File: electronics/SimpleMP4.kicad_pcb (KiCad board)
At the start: 2 copper layers, 126.5 x 65.9 mm, 123 parts, among them J1 USB_OTG, J2 DISPLAY, Q1 8050, Q2 SI2305, Q3 SI2305, Q4 8050, Q5 8550, Q6 SI2305, Q7 8550, U1 OCP8020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

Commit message: added another data bus
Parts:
- removed RN1: 5R, Resistors_THT:R_Array_SIP5
- added R37: 33R, Resistors_SMD:R_0603, F.Cu at (230.8, 226.2)
- added R38: 33R, Resistors_SMD:R_0603, F.Cu at (226.6, 230.7)
- added R39: 33R, Resistors_SMD:R_0603, F.Cu at (235.7, 220.8)
- added R40: 33R, Resistors_SMD:R_0603, F.Cu at (222.6, 235.9)
- added R41: R*, Resistors_SMD:R_0603, F.Cu at (229.8, 231.1)
- added R42: R*, Resistors_SMD:R_0603, F.Cu at (225.8, 235.9)
- added R43: R*, Resistors_SMD:R_0603, F.Cu at (218.0, 242.8)
- added R44: R*, Resistors_SMD:R_0603, F.Cu at (238.9, 220.8)
- added TP1: TEST, Connectors:PINTST, F.Cu at (190.8, 242.5)
- added TP2: TEST, Connectors:PINTST, F.Cu at (219.2, 225.9)
- added TP3: TEST, Connectors:PINTST, F.Cu at (194.5, 242.5)
- added TP4: TEST, Connectors:PINTST, F.Cu at (198.2, 242.5)
- added TP5: TEST, Connectors:PINTST, F.Cu at (232.2, 216.0)
- added TP6: TEST, Connectors:PINTST, F.Cu at (215.1, 232.9)
- added TP7: TEST, Connectors:PINTST, F.Cu at (222.9, 225.9)
- added TP8: TEST, Connectors:PINTST, F.Cu at (219.2, 231.1)
- added TP9: TEST, Connectors:PINTST, F.Cu at (232.2, 221.2)
- B1, B2, B3, B4, B5, B6: footprint SKHLAAA010:SKHLAAA010 -> HP0315AFKP4-R:SW_HP0315AFKP4-R; moved to B.Cu
- moved R36 189.1 mm to (219.3, 236.1)
- moved Q7 179.1 mm to (215.3, 226.8)
- moved B6 176.4 mm to (79.6, 183.0), turned to 270 degrees
- moved R35 173.2 mm to (214.8, 242.8)
- moved C47 169.1 mm to (223.0, 231.0)
- moved C46 164.2 mm to (236.3, 215.9)
- moved C44 163.7 mm to (215.5, 237.9)
- moved B5 160.1 mm to (89.8, 183.0), turned to 270 degrees
- moved U5 159.4 mm to (197.1, 216.8)
- moved C43 157.2 mm to (226.9, 225.8)
- moved B4 143.7 mm to (99.9, 183.0), turned to 270 degrees
- moved B1 133.9 mm to (130.4, 183.0), turned to 90 degrees
- moved B3 127.8 mm to (110.1, 183.0), turned to 270 degrees
- moved B2 115.0 mm to (120.3, 183.0), turned to 270 degrees
- moved J2 95.4 mm to (72.0, 157.6)
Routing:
- net /D0: track 0.00 -> 41.7 mm, vias 0 -> 1
- net /D2: track 0.00 -> 41.6 mm, vias 0 -> 1
- net /D1: track 0.00 -> 40.9 mm, vias 0 -> 1
- net /D3: track 0.00 -> 40.9 mm, vias 0 -> 1
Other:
- board size 126.5 x 65.9 mm -> 130.7 x 66.4 mm

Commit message: routed more of it
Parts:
- moved C43 185.8 mm to (65.4, 134.1), turned to 270 degrees
- moved R35 185.5 mm to (68.2, 129.3), turned to 180 degrees
- moved R36 182.0 mm to (68.1, 134.7), turned to 180 degrees
- moved R39 180.9 mm to (68.6, 151.5), turned to 180 degrees
- moved R44 180.5 mm to (68.6, 161.2), turned to 180 degrees
- moved R37 179.8 mm to (68.6, 148.5), turned to 180 degrees
- moved R41 177.6 mm to (68.6, 156.6), turned to 180 degrees
- moved R38 177.5 mm to (68.6, 150.0), turned to 180 degrees
- moved R42 175.4 mm to (68.6, 158.1), turned to 180 degrees
- moved Q7 175.0 mm to (68.2, 132.1)
- moved R40 174.9 mm to (68.6, 153.0), turned to 180 degrees
- moved R43 171.1 mm to (68.6, 159.6), turned to 180 degrees
- moved U5 13.6 mm to (183.5, 218.1)
- moved C3 3.44 mm to (112.6, 153.4), turned to 90 degrees
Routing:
- net /LCDRDN: track 0.00 -> 116.9 mm, vias 0 -> 2
- net /LCDWRN: track 0.00 -> 114.1 mm, vias 0 -> 2
- net /FALE/RS/A1: track 43.0 -> 149.8 mm, vias 2 -> 3
- net /LCDCSN: track 0.00 -> 105.5 mm, vias 0 -> 2
- net /D8: track 39.2 -> 115.2 mm, vias 2 -> 3
- net /D9: track 41.1 -> 115.1 mm, vias 2 -> 3
- net /D10: track 42.7 -> 114.6 mm, vias 2 -> 3
- net /D11: track 42.1 -> 112.5 mm, vias 2 -> 3
- net /D12: track 42.7 -> 110.3 mm, vias 2 -> 3
- net /D13: track 44.6 -> 110.7 mm, vias 2 -> 3
- net /D14: track 46.3 -> 110.0 mm, vias 2 -> 3
- net /D15: track 48.0 -> 109.6 mm, vias 2 -> 3
- net /D6: track 0.00 -> 52.4 mm, vias 0 -> 2
- net /D5: track 0.00 -> 52.0 mm, vias 0 -> 2
- net /D7: track 0.00 -> 47.2 mm, vias 0 -> 2
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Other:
- board size 130.7 x 66.4 mm -> 136.9 x 66.4 mm

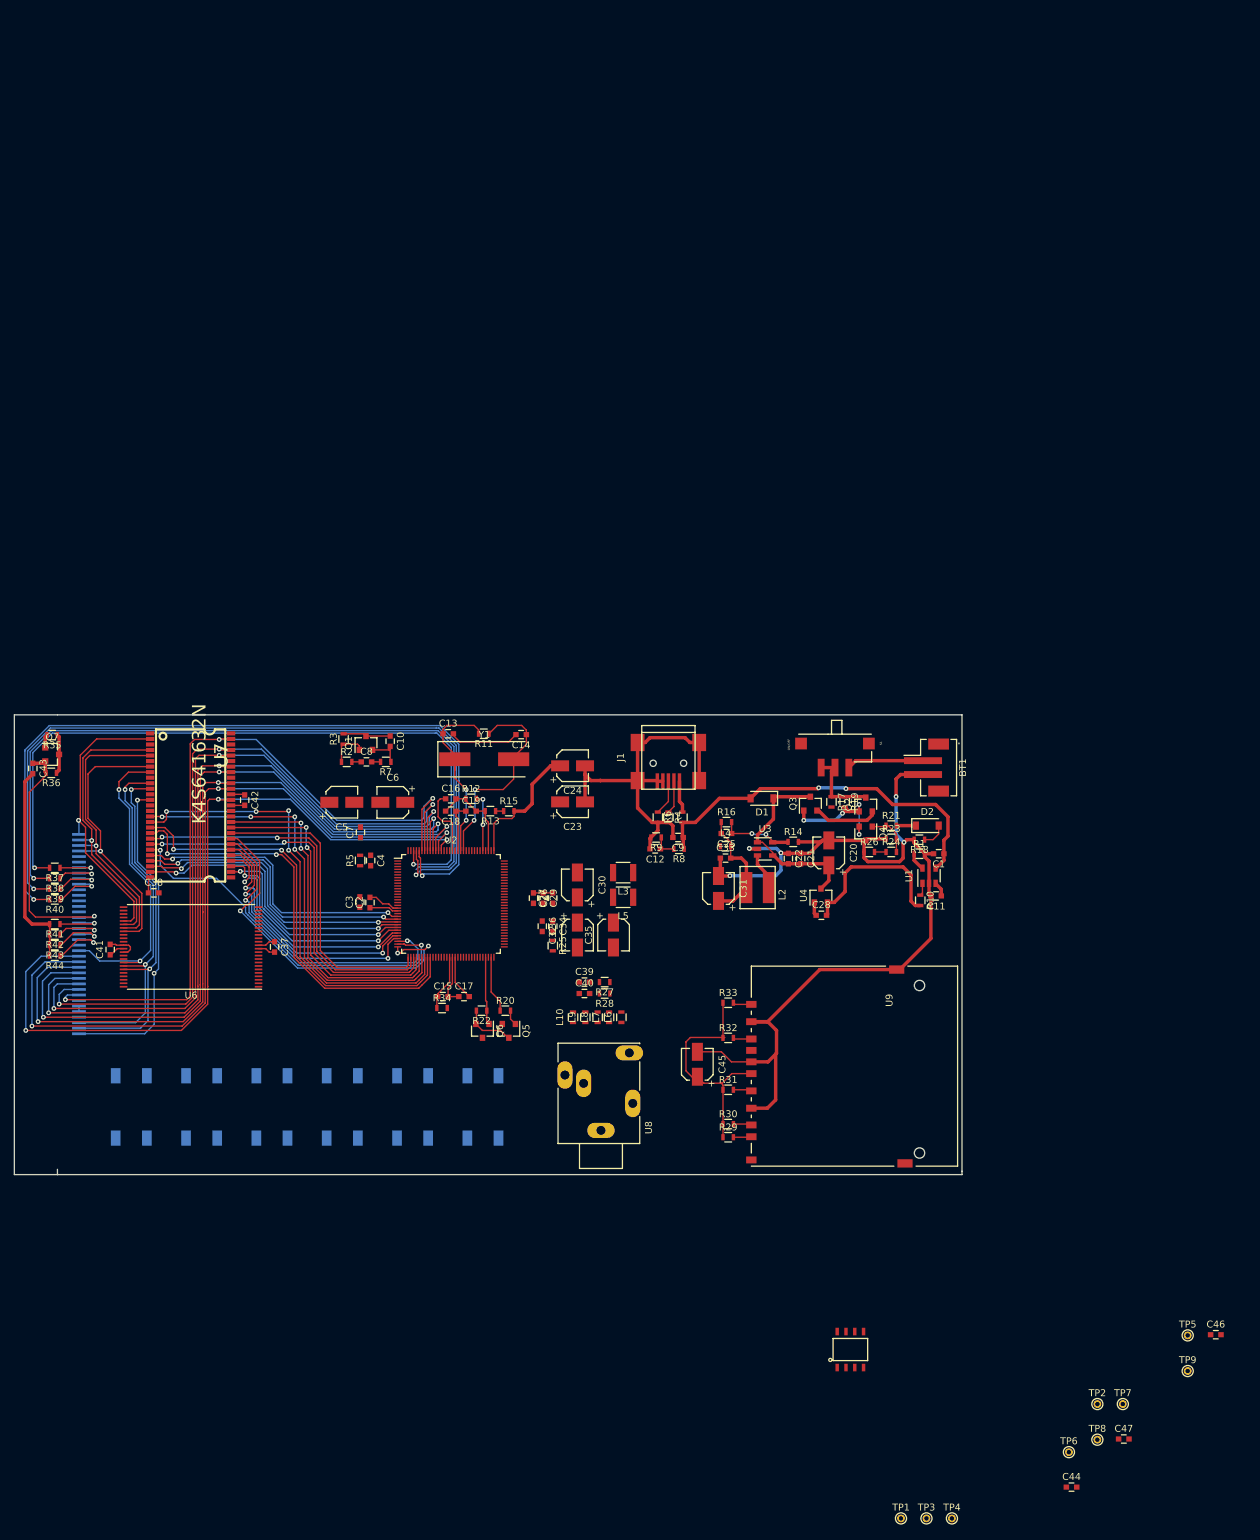
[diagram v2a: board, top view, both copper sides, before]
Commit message: routed more of the segments
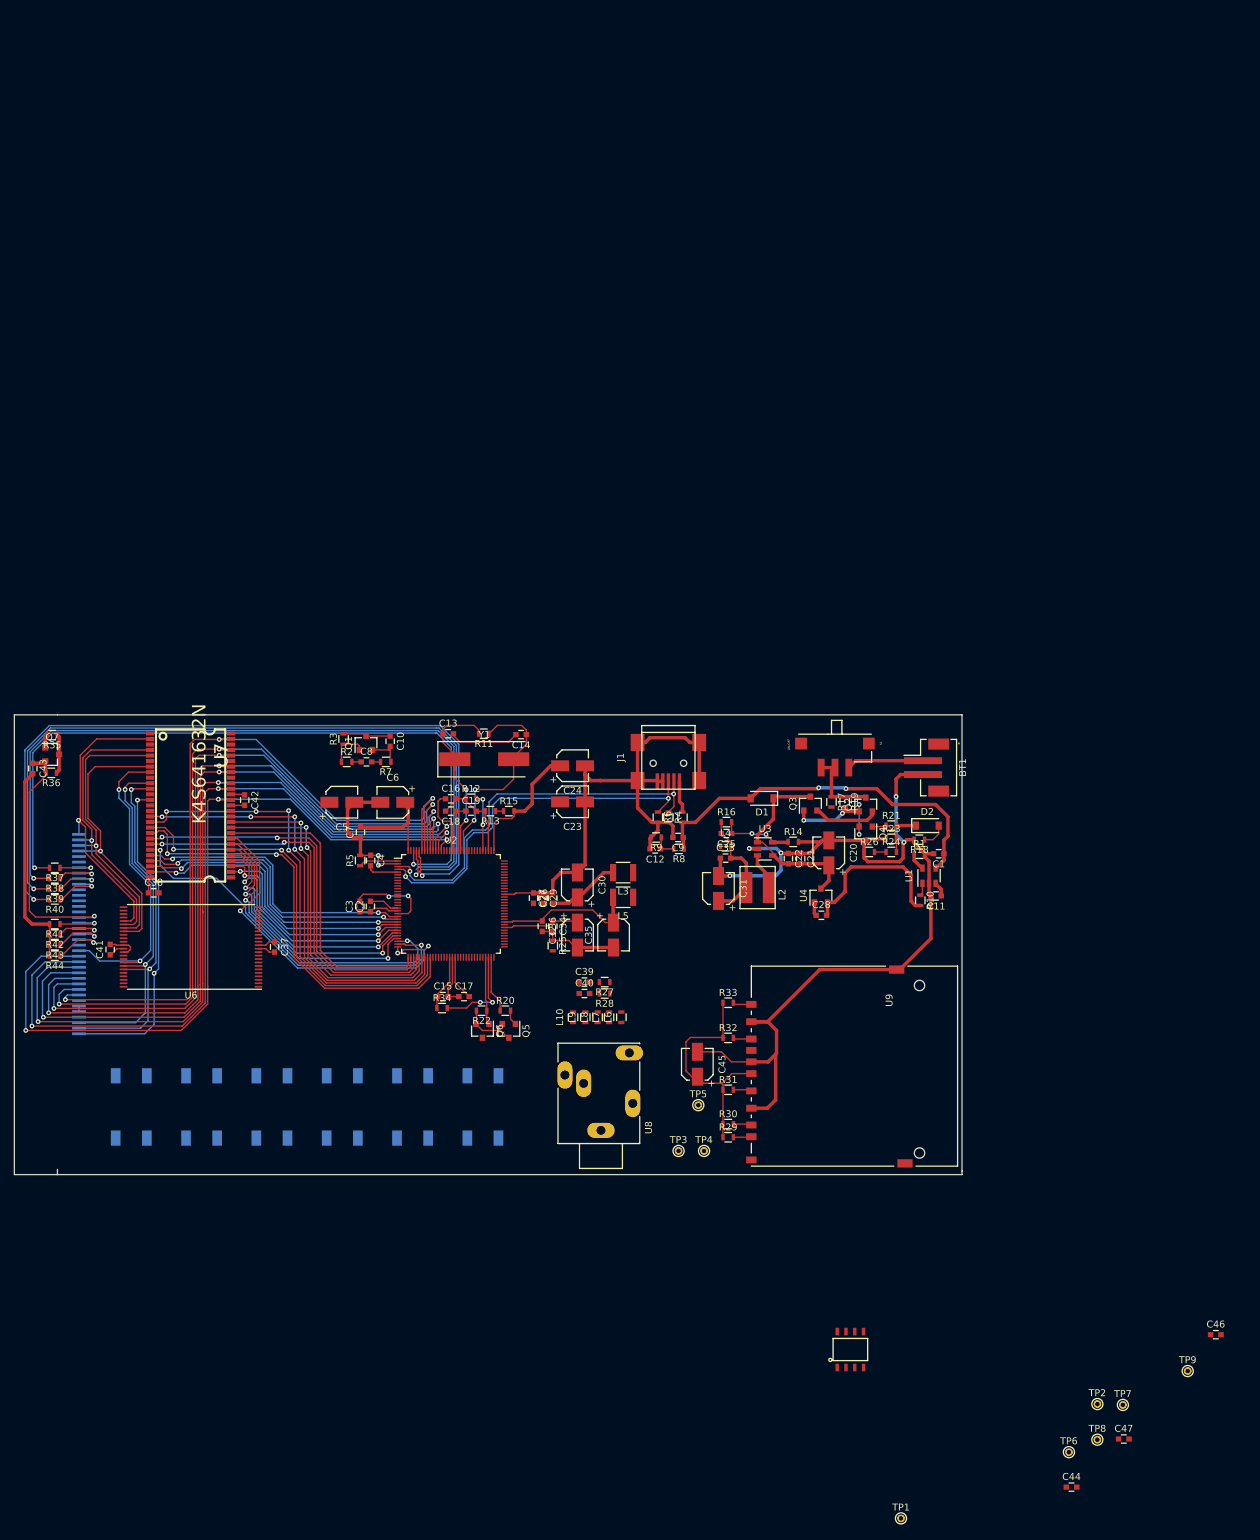
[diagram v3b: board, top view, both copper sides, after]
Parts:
- moved TP5 78.1 mm to (161.5, 182.8)
- moved TP3 64.0 mm to (158.7, 189.4)
- moved TP4 64.0 mm to (162.4, 189.4)
- moved C3 0.63 mm to (112.6, 154.1)
- moved C2 0.58 mm to (114.2, 154.1)
- moved TP7 0.13 mm to (222.9, 226.1)
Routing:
- net GND: track 254.5 -> 309.1 mm, vias 5 -> 7
- net /DM: track 4.78 -> 56.0 mm, vias 0 -> 2
- net /DP: track 5.08 -> 54.8 mm, vias 0 -> 2
- net Net-(C35-Pad1): track 0.00 -> 21.1 mm
- net Net-(C6-Pad1): track 0.00 -> 17.0 mm
- net VCC: track 92.6 -> 109.5 mm, vias 0 -> 2
- net /SD_DET: track 0.00 -> 13.7 mm, vias 0 -> 2
- net Net-(C32-Pad1): track 0.00 -> 11.0 mm
- net Net-(C27-Pad1): track 0.00 -> 10.5 mm
- net Net-(R5-Pad1): track 0.00 -> 5.71 mm

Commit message: added routing to buttons
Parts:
- removed TP1, TP2, TP3, TP4, TP5, TP6, TP7, TP8, TP9: TEST, Connectors:PINTST
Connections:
- U2 pad 46: /SDDCLK -> /SDCLK
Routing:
- net /KIN0: track 0.00 -> 65.4 mm, vias 0 -> 3
- net /KIN1: track 0.00 -> 56.0 mm, vias 0 -> 3
- net /KIN2: track 0.00 -> 46.8 mm, vias 0 -> 3
- net /KIN3: track 0.00 -> 37.4 mm, vias 0 -> 3
- net /KIN4: track 0.00 -> 28.3 mm, vias 0 -> 3
- net /LCDRDN: track 116.9 -> 94.9 mm, vias 2 -> 1
- net /PLAY_ON: track 3.59 -> 25.4 mm, vias 0 -> 1
- net /FALE/RS/A1: track 149.8 -> 158.9 mm, vias 3 -> 4
- net /LCDWRN: track 114.1 -> 112.8 mm

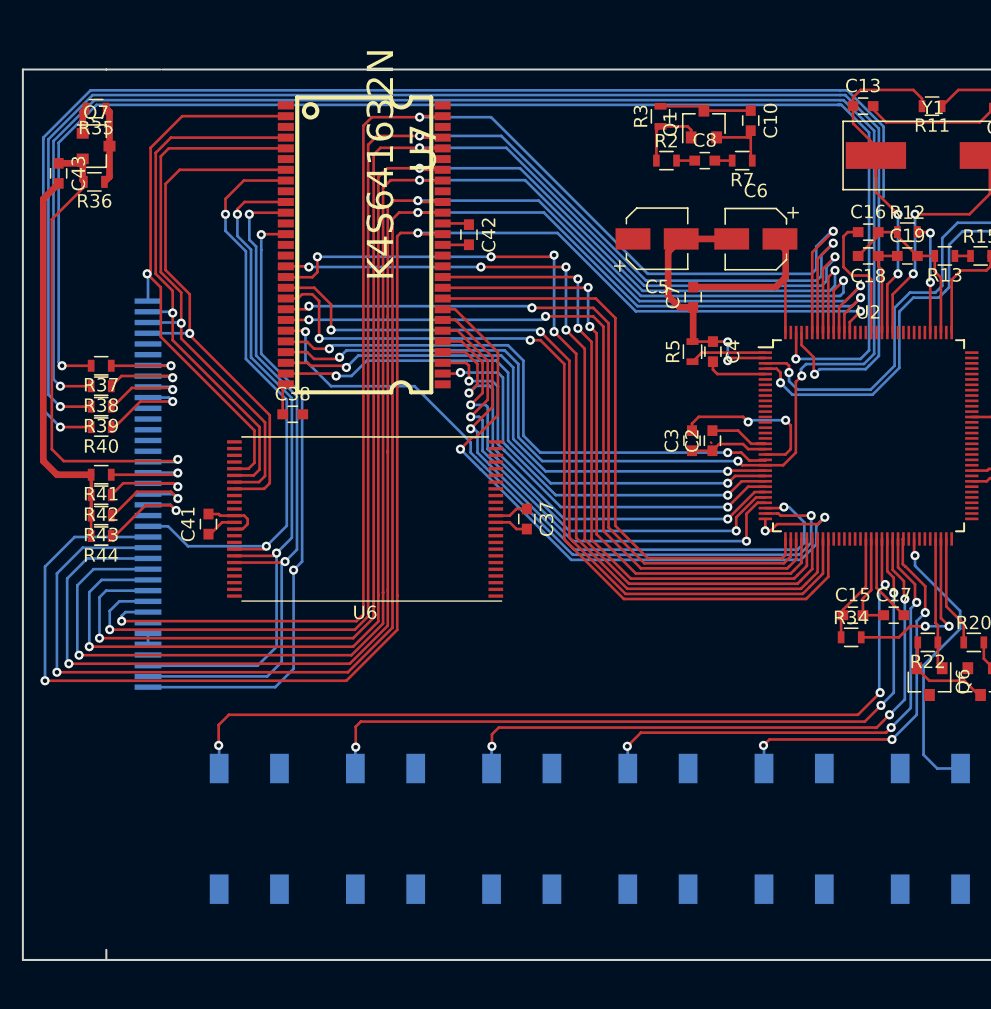
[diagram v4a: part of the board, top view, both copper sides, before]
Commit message: 94 unconnected left
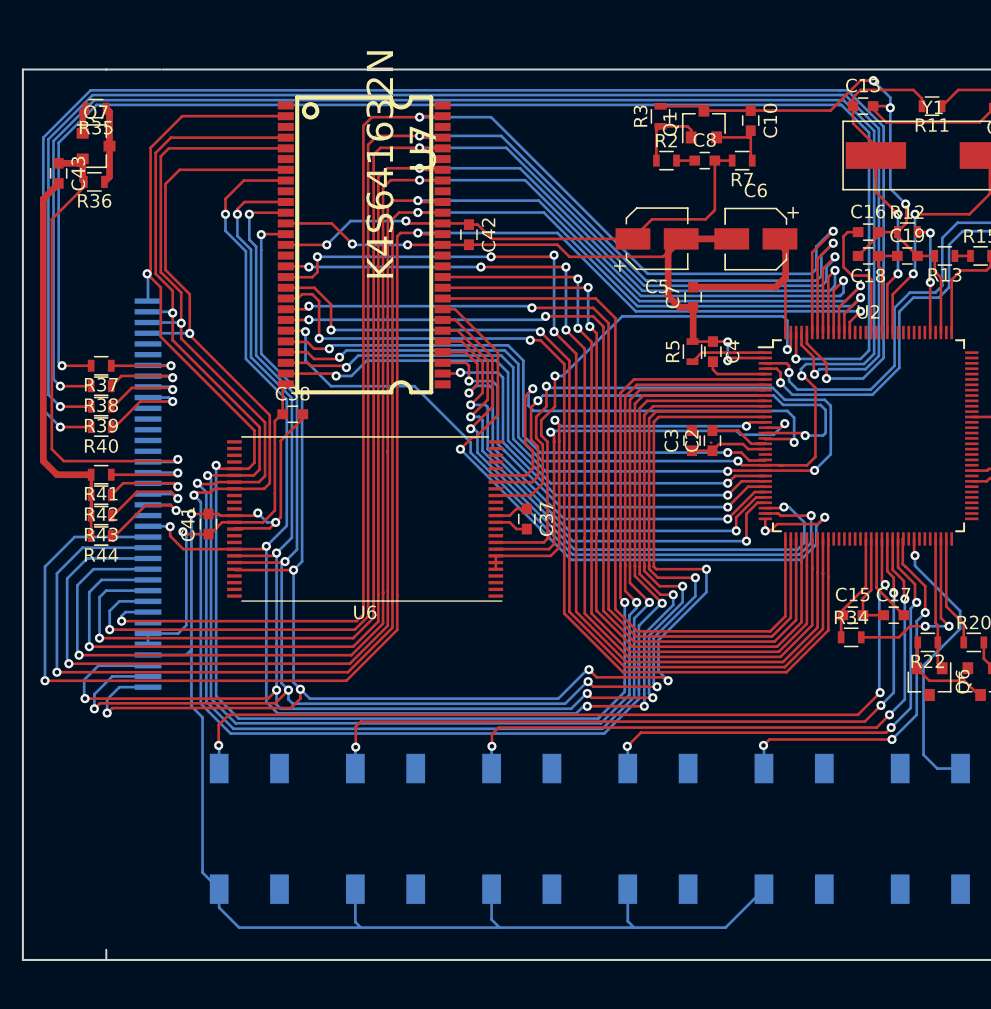
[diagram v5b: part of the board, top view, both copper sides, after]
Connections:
- U6 pad 14: /I2C_SDA -> Net-(U6-Pad14)
- U6 pad 15: /I2C_SCL -> Net-(U6-Pad15)
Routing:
- net GND: track 309.1 -> 462.6 mm, vias 7 -> 15
- net /D3: track 40.9 -> 128.3 mm, vias 1 -> 3
- net /D2: track 41.6 -> 128.5 mm, vias 1 -> 3
- net /D1: track 40.9 -> 126.3 mm, vias 1 -> 3
- net /D0: track 41.7 -> 126.1 mm, vias 1 -> 3
- net /D5: track 52.0 -> 130.1 mm, vias 2 -> 7
- net /D7: track 47.2 -> 124.3 mm, vias 2 -> 7
- net /D6: track 52.4 -> 127.6 mm, vias 2 -> 7
- net /D4: track 45.4 -> 118.2 mm, vias 2 -> 6
- net VCC: track 109.5 -> 156.1 mm, vias 2 -> 3
- net /FCLE/A2: track 43.0 -> 85.5 mm, vias 2 -> 4
- net /FCE0: track 0.00 -> 39.8 mm, vias 0 -> 2
- net /FWEN: track 0.00 -> 37.9 mm, vias 0 -> 2
- net /FWP: track 0.00 -> 35.3 mm, vias 0 -> 2
- net /FREN: track 0.00 -> 32.6 mm, vias 0 -> 2
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
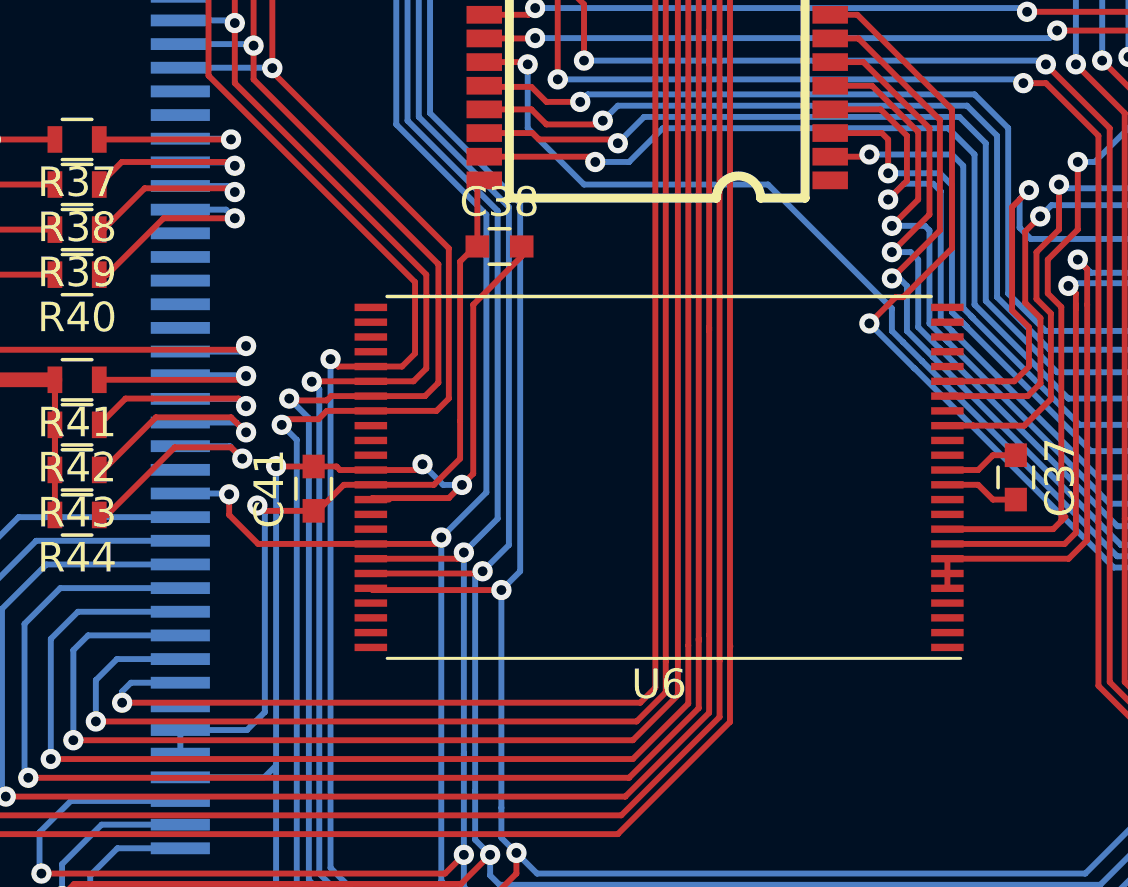
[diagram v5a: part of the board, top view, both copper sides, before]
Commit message: routed more connections
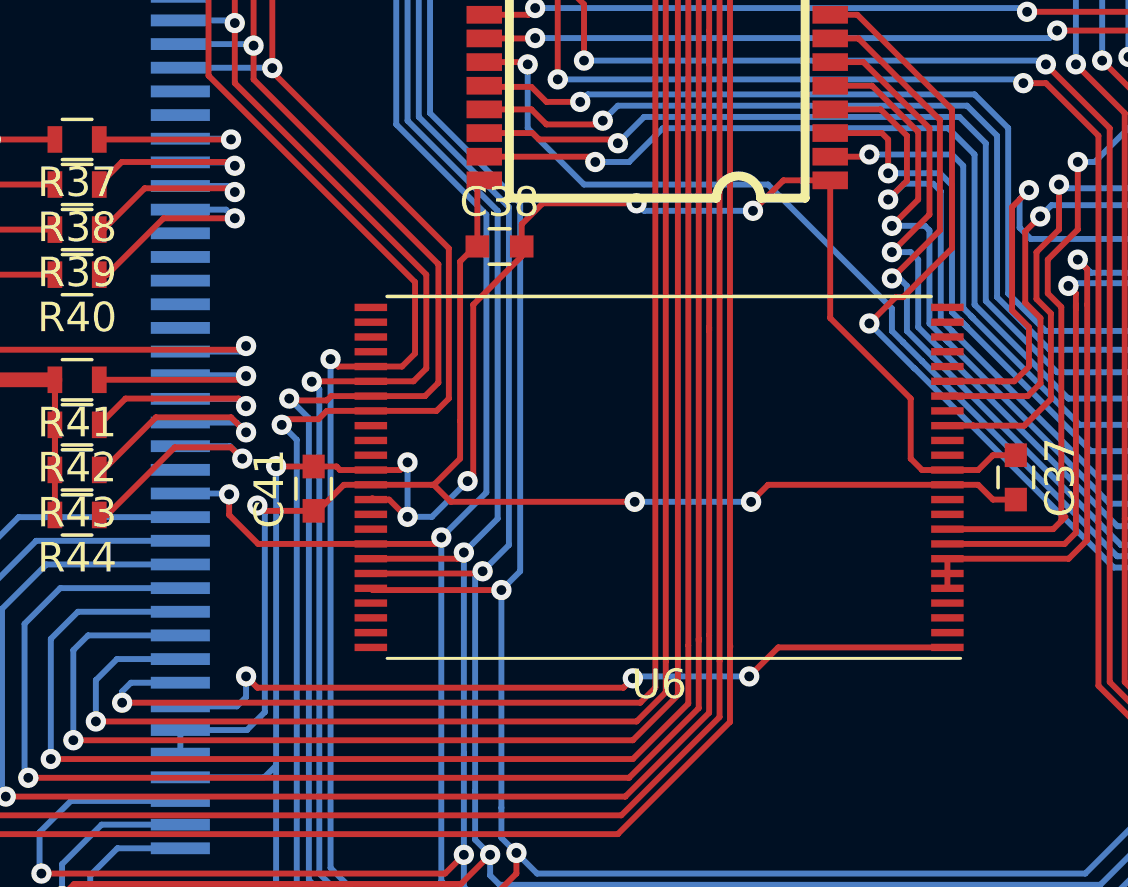
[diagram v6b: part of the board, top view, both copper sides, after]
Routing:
- net /RESETN: track 5.23 -> 32.7 mm, vias 0 -> 3
- net GND: track 462.6 -> 486.2 mm, vias 15 -> 18
- net VCC: track 156.1 -> 174.1 mm, vias 3 -> 5
